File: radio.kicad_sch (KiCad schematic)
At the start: 39 parts

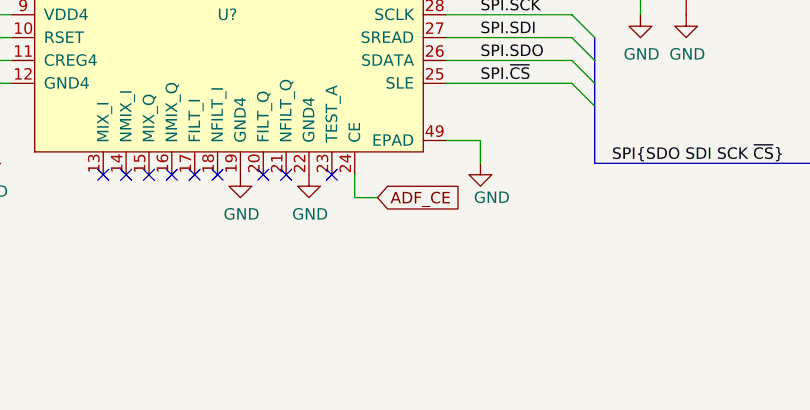
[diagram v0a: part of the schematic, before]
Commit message: Connected ADF7021 chip enable to MCU, grouped PTT/W_DISABLE signal with SWDIO
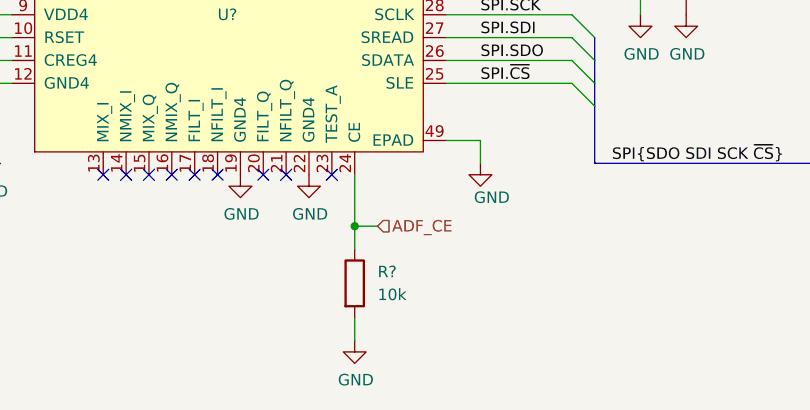
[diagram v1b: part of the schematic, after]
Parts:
- added R?: 10k, Resistor_SMD:R_0402_1005Metric, symbol Device:R
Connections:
- net ADF_CE: now also R?.1
- net GND: now also R?.2
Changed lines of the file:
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@@
   (junction (at 182.88 69.85) (diameter 0) (color 0 0 0 0)
+  )
+  (junction (at 177.8 141.605) (diameter 0) (color 0 0 0 0)
   )
   (junction (at 119.38 90.17) (diameter 0) (color 0 0 0 0)
@@
     (stroke (width 0) (type default) (color 0 0 0 0))
   )
+  (wire (pts (xy 177.8 141.605) (xy 177.8 144.145))
+    (stroke (width 0) (type default) (color 0 0 0 0))
+  )
   (wire (pts (xy 203.2 110.49) (xy 203.2 115.57))
     (stroke (width 0) (type default) (color 0 0 0 0))
@@
     (stroke (width 0) (type default) (color 0 0 0 0))
   )
-  (wire (pts (xy 177.8 138.43) (xy 180.34 138.43))
-    (stroke (width 0) (type default) (color 0 0 0 0))
-  )
   (wire (pts (xy 173.99 67.31) (xy 173.99 68.58))
     (stroke (width 0) (type default) (color 0 0 0 0))
@@
     (stroke (width 0) (type default) (color 0 0 0 0))
   )
+  (wire (pts (xy 177.8 141.605) (xy 180.34 141.605))
+    (stroke (width 0) (type default) (color 0 0 0 0))
+  )
   (wire (pts (xy 135.89 86.36) (xy 135.89 100.33))
     (stroke (width 0) (type default) (color 0 0 0 0))
@@
     (stroke (width 0) (type default) (color 0 0 0 0))
   )
-  (wire (pts (xy 177.8 135.89) (xy 177.8 138.43))
-    (stroke (width 0) (type default) (color 0 0 0 0))
-  )
   (bus (pts (xy 204.47 125.73) (xy 204.47 128.27))
     (stroke (width 0) (type default) (color 0 0 0 0))
@@
     (stroke (width 0) (type default) (color 0 0 0 0))
   )
+  (wire (pts (xy 177.8 151.765) (xy 177.8 154.305))
+    (stroke (width 0) (type default) (color 0 0 0 0))
+  )
   (wire (pts (xy 104.14 125.73) (xy 104.14 115.57))
     (stroke (width 0) (type default) (color 0 0 0 0))
@@
   )
   (wire (pts (xy 198.12 110.49) (xy 203.2 110.49))
+    (stroke (width 0) (type default) (color 0 0 0 0))
+  )
+  (wire (pts (xy 177.8 135.89) (xy 177.8 141.605))
     (stroke (width 0) (type default) (color 0 0 0 0))
   )
@@
     )
   )
-  (global_label "ADF_CE" (shape input) (at 180.34 138.43 0) (fields_autoplaced)
-    (effects (font (size 1.27 1.27)) (justify left))
-    (property "Intersheet References" "${INTERSHEET_REFS}" (id 0) (at 189.498 138.3506 0)
-      (effects (font (size 1.27 1.27)) (justify left) hide)
-    )
-  )
   (global_label "RF_IN" (shape input) (at 86.36 110.49 180) (fields_autoplaced)
     (effects (font (size 1.27 1.27)) (justify right))
@@
     (effects (font (size 1.27 1.27)) (justify right))
   )
+  (hierarchical_label "ADF_CE" (shape input) (at 180.34 141.605 0)
+    (effects (font (size 1.27 1.27)) (justify left))
+  )
   (hierarchical_label "MOD1" (shape input) (at 100.33 50.8 180)
     (effects (font (size 1.27 1.27)) (justify right))
@@
     (pin "1")
     (pin "2")
+  )
+  (symbol (lib_id "power:GND") (at 177.8 154.305 0) (unit 1)
+    (in_bom yes) (on_board yes)
+    (property "Reference" "#PWR?" (id 0) (at 177.8 160.655 0)
+      (effects (font (size 1.27 1.27)) hide)
+    )
+    (property "Value" "GND" (id 1) (at 177.927 158.6992 0))
+    (property "Footprint" "" (id 2) (at 177.8 154.305 0)
+      (effects (font (size 1.27 1.27)) hide)
+    )
+    (property "Datasheet" "" (id 3) (at 177.8 154.305 0)
+      (effects (font (size 1.27 1.27)) hide)
+    )
+    (pin "1")
   )
   (symbol (lib_id "Device:R") (at 109.22 50.8 270) (unit 1)
@@
     (pin "1")
   )
+  (symbol (lib_id "Device:R") (at 177.8 147.955 0) (unit 1)
+    (in_bom yes) (on_board yes)
+    (property "Reference" "R?" (id 0) (at 180.34 146.685 0)
+      (effects (font (size 1.27 1.27)) (justify left))
+    )
+    (property "Value" "10k" (id 1) (at 180.34 149.225 0)
+      (effects (font (size 1.27 1.27)) (justify left))
+    )
+    (property "Footprint" "Resistor_SMD:R_0402_1005Metric" (id 2) (at 176.022 147.955 90)
+      (effects (font (size 1.27 1.27)) hide)
+    )
+    (property "Datasheet" "~" (id 3) (at 177.8 147.955 0)
+      (effects (font (size 1.27 1.27)) hide)
+    )
+    (pin "1")
+    (pin "2")
+  )
   (symbol (lib_id "power:+3V3") (at 110.49 87.63 0) (unit 1)

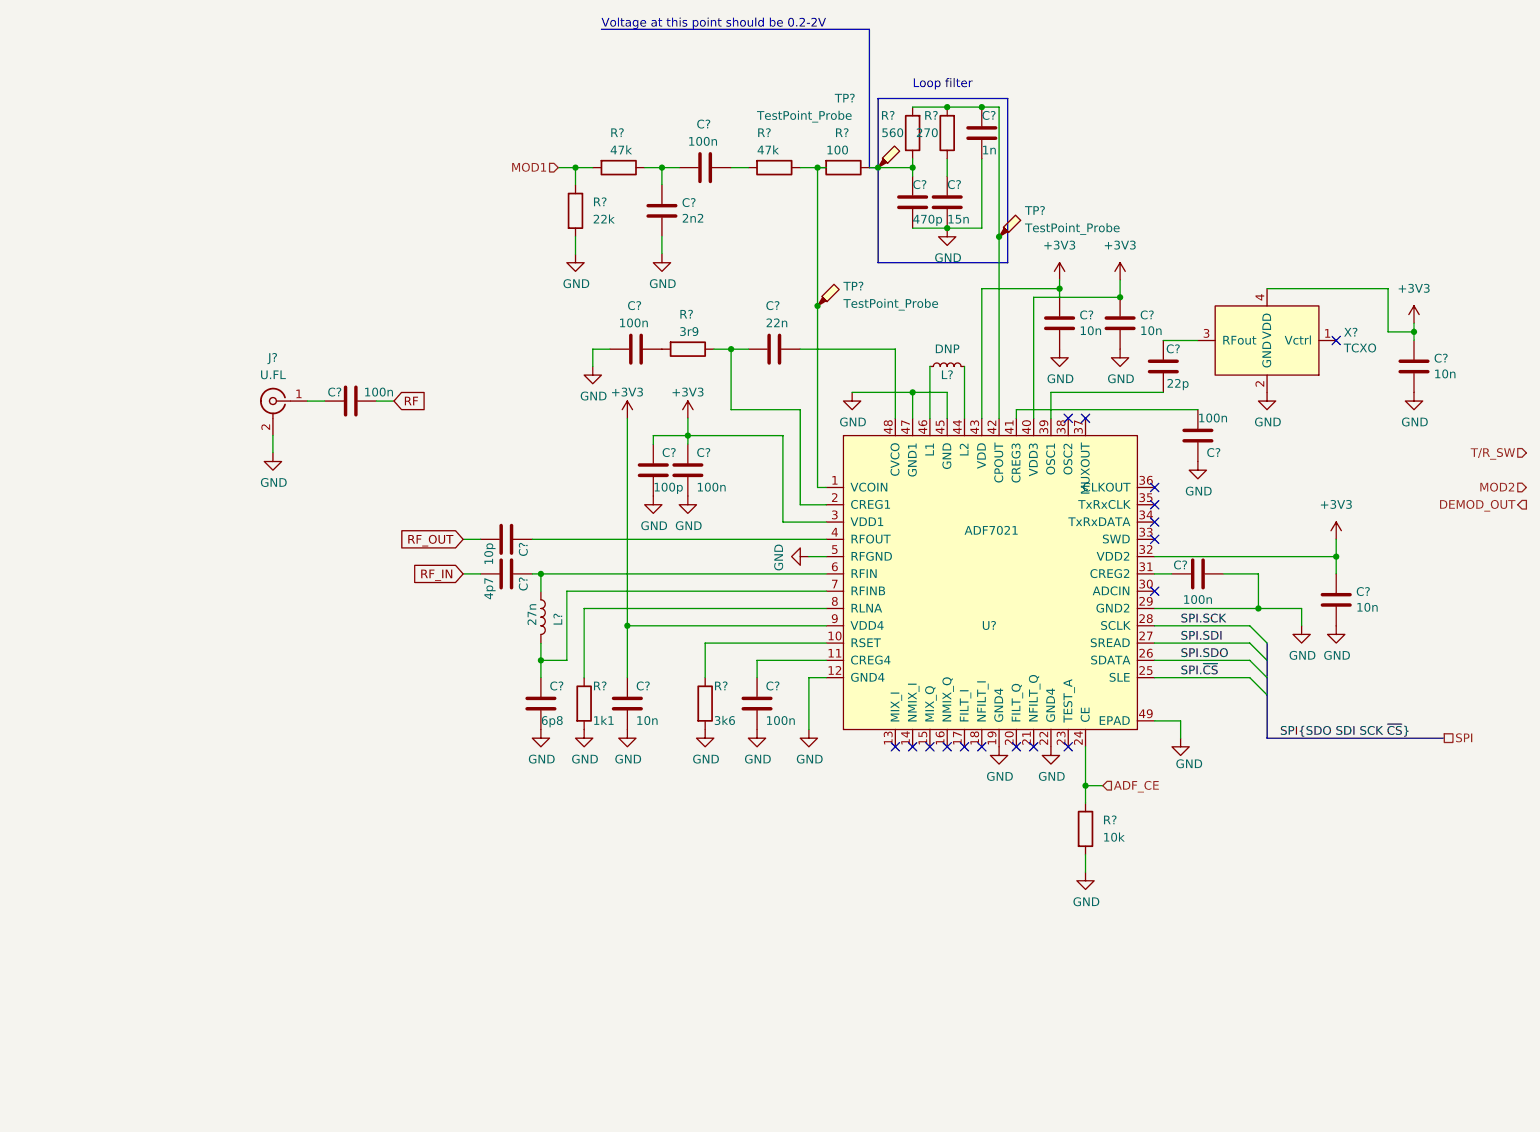
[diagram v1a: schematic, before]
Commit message: Set up ADF7021 for single RF output, 2-point modulation
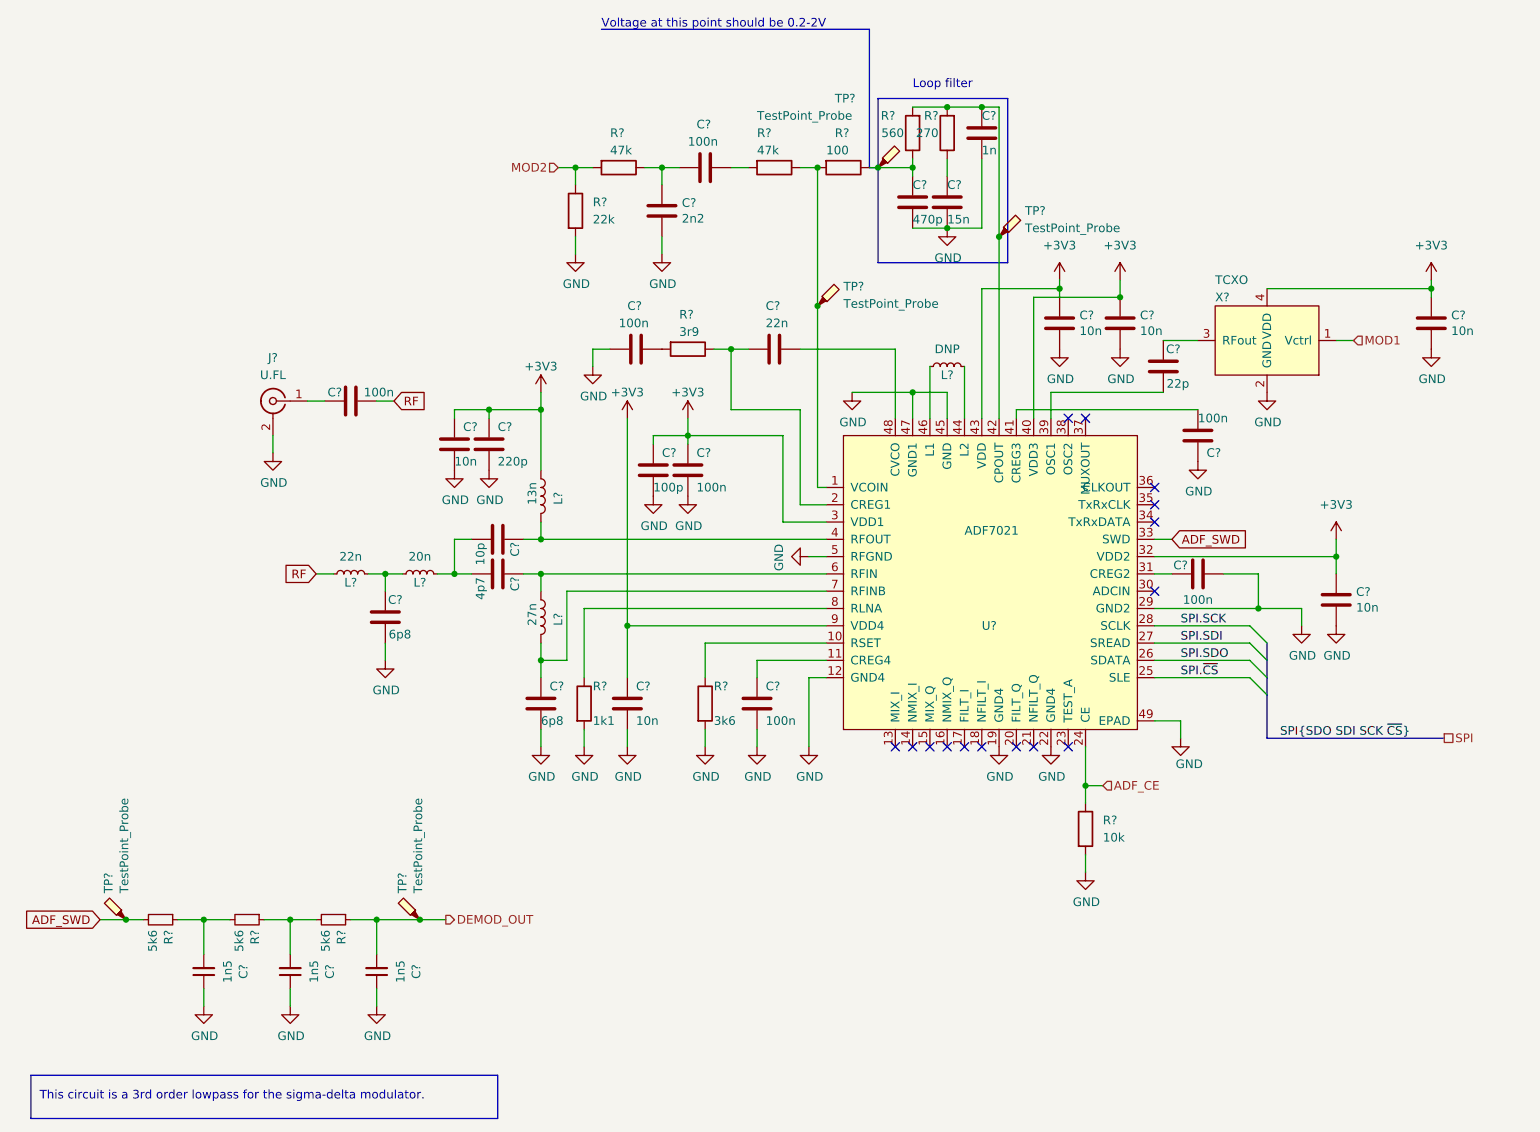
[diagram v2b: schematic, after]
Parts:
- added C?: 6p8, Capacitor_SMD:C_0402_1005Metric, symbol Device:C
- added C? (x3): 1n5, Capacitor_SMD:C_0603_1608Metric, symbol Mainboard-rescue:C_Small-Device
- added C?: 10n, Capacitor_SMD:C_0402_1005Metric, symbol Device:C
- added C?: 220p, Capacitor_SMD:C_0402_1005Metric, symbol Device:C
- added L?: 20n, Inductor_SMD:L_0603_1608Metric, symbol Device:L_Small
- added L?: 22n, Inductor_SMD:L_0603_1608Metric, symbol Device:L_Small
- added L?: 13n, Inductor_SMD:L_0402_1005Metric, symbol Device:L
- added R? (x3): 5k6, Resistor_SMD:R_0603_1608Metric, symbol Mainboard-rescue:R_Small-device
- added TP? (x2): TestPoint_Probe, TestPoint:TestPoint_Pad_D1.0mm, symbol Mainboard-rescue:TestPoint_Probe-Connector
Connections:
- net RF_OUT is gone; now on an unnamed net: C?.1
- net +3V3: now also C?.1, C?.1, L?.1
- net DEMOD_OUT: now also C?.2, R?.1, TP?.1
- net GND: now also C?.1, C?.1, C?.1, C?.1, C?.2, C?.2
- net MOD1: now also X?.1 (Vctrl); no longer R?.1, R?.2
- net MOD2: now also R?.1, R?.2
- net RF: now also L?.1
- net at C?.2, U?.4 (RFOUT): now also L?.2
- net ADF_SWD: now reaches U?.33 (SWD)
- net ADF_SWD: now also R?.2, TP?.1
- net RF_IN: no longer names the net of C?.1
- net RF_IN: now also L?.2
- new net: C?.2, L?.1, L?.2
- new net: C?.2, R?.1, R?.2 (x2)
- no-connect marks 17 -> 15
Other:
- note added: "This circuit is a 3rd order lowpass for the sigma-delta modulator."
- moved on the sheet: C?

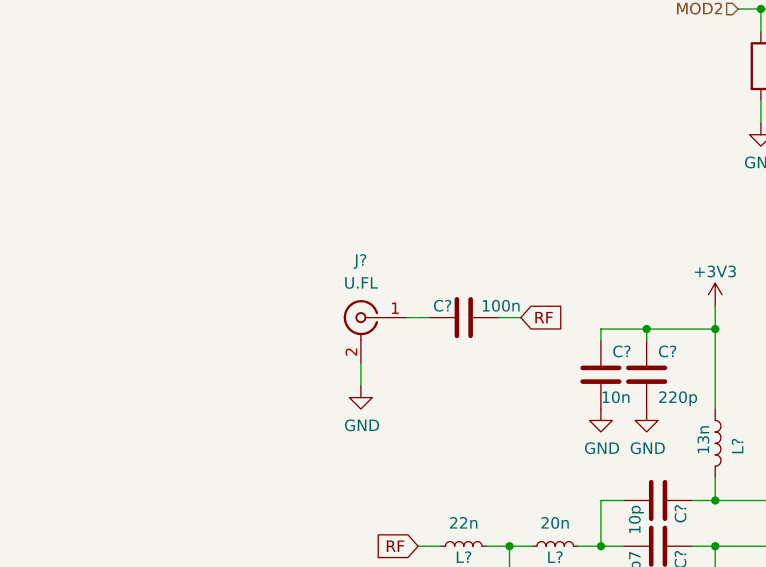
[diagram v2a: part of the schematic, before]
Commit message: Replaced U.FL RF connector with MHF4
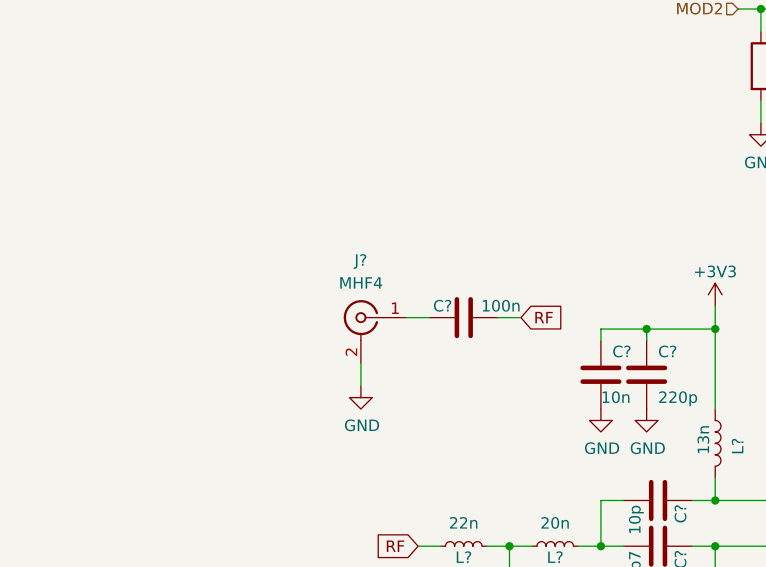
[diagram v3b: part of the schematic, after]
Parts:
- J?: value U.FL -> MHF4; footprint Connector_Coaxial:U.FL_Hirose_U.FL-R-SMT-1_Vertical -> dvk-mx8m-bsb:MHF4_20449-001E
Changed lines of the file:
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@@
     (in_bom yes) (on_board yes)
     (property "Reference" "J?" (id 0) (at 58.42 78.74 0))
-    (property "Value" "U.FL" (id 1) (at 58.42 81.28 0))
-    (property "Footprint" "Connector_Coaxial:U.FL_Hirose_U.FL-R-SMT-1_Vertical" (id 2) (at 58.42 85.09 0)
+    (property "Value" "MHF4" (id 1) (at 58.42 81.28 0))
+    (property "Footprint" "dvk-mx8m-bsb:MHF4_20449-001E" (id 2) (at 58.42 85.09 0)
       (effects (font (size 1.27 1.27)) hide)
     )

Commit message: Set all SMD passive size to 0402
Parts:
- C? (x3): footprint Capacitor_SMD:C_0603_1608Metric -> Capacitor_SMD:C_0402_1005Metric
- L? (x3): footprint Inductor_SMD:L_0603_1608Metric -> Inductor_SMD:L_0402_1005Metric
- R? (x3): footprint Resistor_SMD:R_0603_1608Metric -> Resistor_SMD:R_0402_1005Metric
- TP? (x3): footprint (none) -> TestPoint:TestPoint_Pad_D1.0mm
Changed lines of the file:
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@@
     (property "Reference" "L?" (id 0) (at 80.01 111.76 90))
     (property "Value" "20n" (id 1) (at 80.01 107.95 90))
-    (property "Footprint" "Inductor_SMD:L_0603_1608Metric" (id 2) (at 80.01 110.49 0)
+    (property "Footprint" "Inductor_SMD:L_0402_1005Metric" (id 2) (at 80.01 110.49 0)
       (effects (font (size 1.27 1.27)) hide)
     )
@@
       (effects (font (size 1.27 1.27)) (justify left))
     )
-    (property "Footprint" "Resistor_SMD:R_0603_1608Metric" (id 2) (at 41.91 161.29 0)
+    (property "Footprint" "Resistor_SMD:R_0402_1005Metric" (id 2) (at 41.91 161.29 0)
       (effects (font (size 1.27 1.27)) hide)
     )
@@
     (property "Reference" "C?" (id 0) (at 66.7766 168.91 90))
     (property "Value" "1n5" (id 1) (at 64.4652 168.91 90))
-    (property "Footprint" "Capacitor_SMD:C_0603_1608Metric" (id 2) (at 60.96 168.91 0)
+    (property "Footprint" "Capacitor_SMD:C_0402_1005Metric" (id 2) (at 60.96 168.91 0)
       (effects (font (size 1.27 1.27)) hide)
     )
@@
       (effects (font (size 1.27 1.27)) (justify left))
     )
-    (property "Footprint" "" (id 2) (at 152.4 50.8 0)
+    (property "Footprint" "TestPoint:TestPoint_Pad_D1.0mm" (id 2) (at 152.4 50.8 0)
       (effects (font (size 1.27 1.27)) hide)
     )
@@
       (effects (font (size 1.27 1.27)) (justify left))
     )
-    (property "Footprint" "Resistor_SMD:R_0603_1608Metric" (id 2) (at 54.61 161.29 0)
+    (property "Footprint" "Resistor_SMD:R_0402_1005Metric" (id 2) (at 54.61 161.29 0)
       (effects (font (size 1.27 1.27)) hide)
     )
@@
     (property "Reference" "C?" (id 0) (at 54.0766 168.91 90))
     (property "Value" "1n5" (id 1) (at 51.7652 168.91 90))
-    (property "Footprint" "Capacitor_SMD:C_0603_1608Metric" (id 2) (at 48.26 168.91 0)
+    (property "Footprint" "Capacitor_SMD:C_0402_1005Metric" (id 2) (at 48.26 168.91 0)
       (effects (font (size 1.27 1.27)) hide)
     )
@@
     (property "Reference" "C?" (id 0) (at 79.4766 168.91 90))
     (property "Value" "1n5" (id 1) (at 77.1652 168.91 90))
-    (property "Footprint" "Capacitor_SMD:C_0603_1608Metric" (id 2) (at 73.66 168.91 0)
+    (property "Footprint" "Capacitor_SMD:C_0402_1005Metric" (id 2) (at 73.66 168.91 0)
       (effects (font (size 1.27 1.27)) hide)
     )
@@
     (property "Reference" "L?" (id 0) (at 69.85 111.76 90))
     (property "Value" "22n" (id 1) (at 69.85 107.95 90))
-    (property "Footprint" "Inductor_SMD:L_0603_1608Metric" (id 2) (at 69.85 110.49 0)
+    (property "Footprint" "Inductor_SMD:L_0402_1005Metric" (id 2) (at 69.85 110.49 0)
       (effects (font (size 1.27 1.27)) hide)
     )
@@
       (effects (font (size 1.27 1.27)) (justify left))
     )
-    (property "Footprint" "" (id 2) (at 143.51 71.12 0)
+    (property "Footprint" "TestPoint:TestPoint_Pad_D1.0mm" (id 2) (at 143.51 71.12 0)
       (effects (font (size 1.27 1.27)) hide)
     )
@@
       (effects (font (size 1.27 1.27)) (justify left))
     )
-    (property "Footprint" "" (id 2) (at 170.18 60.96 0)
+    (property "Footprint" "TestPoint:TestPoint_Pad_D1.0mm" (id 2) (at 170.18 60.96 0)
       (effects (font (size 1.27 1.27)) hide)
     )
@@
       (effects (font (size 1.27 1.27)) (justify left))
     )
-    (property "Footprint" "Resistor_SMD:R_0603_1608Metric" (id 2) (at 67.31 161.29 0)
+    (property "Footprint" "Resistor_SMD:R_0402_1005Metric" (id 2) (at 67.31 161.29 0)
       (effects (font (size 1.27 1.27)) hide)
     )
@@
     (property "Reference" "L?" (id 0) (at 157.48 81.28 90))
     (property "Value" "DNP" (id 1) (at 157.48 77.47 90))
-    (property "Footprint" "Inductor_SMD:L_0603_1608Metric" (id 2) (at 157.48 80.01 0)
-      (effects (font (size 1.27 1.27)) hide)
-    )
+    (property "Footprint" "Inductor_SMD:L_0402_1005Metric" (id 2) (at 157.48 80.01 0)
+      (effects (font (size 1.27 1.27)) hide)
+    )
